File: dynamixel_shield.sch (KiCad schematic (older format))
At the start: 23 parts, among them P1 BARREL_JACK, P2 CONN_01X02, P3 CONN_01X03, P4 CONN_01X03, P5 CONN_01X03, P6 CONN_01X03, P7 CONN_01X03, P8 CONN_01X03, P9 CONN_01X03, Q1 MOSFET_N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

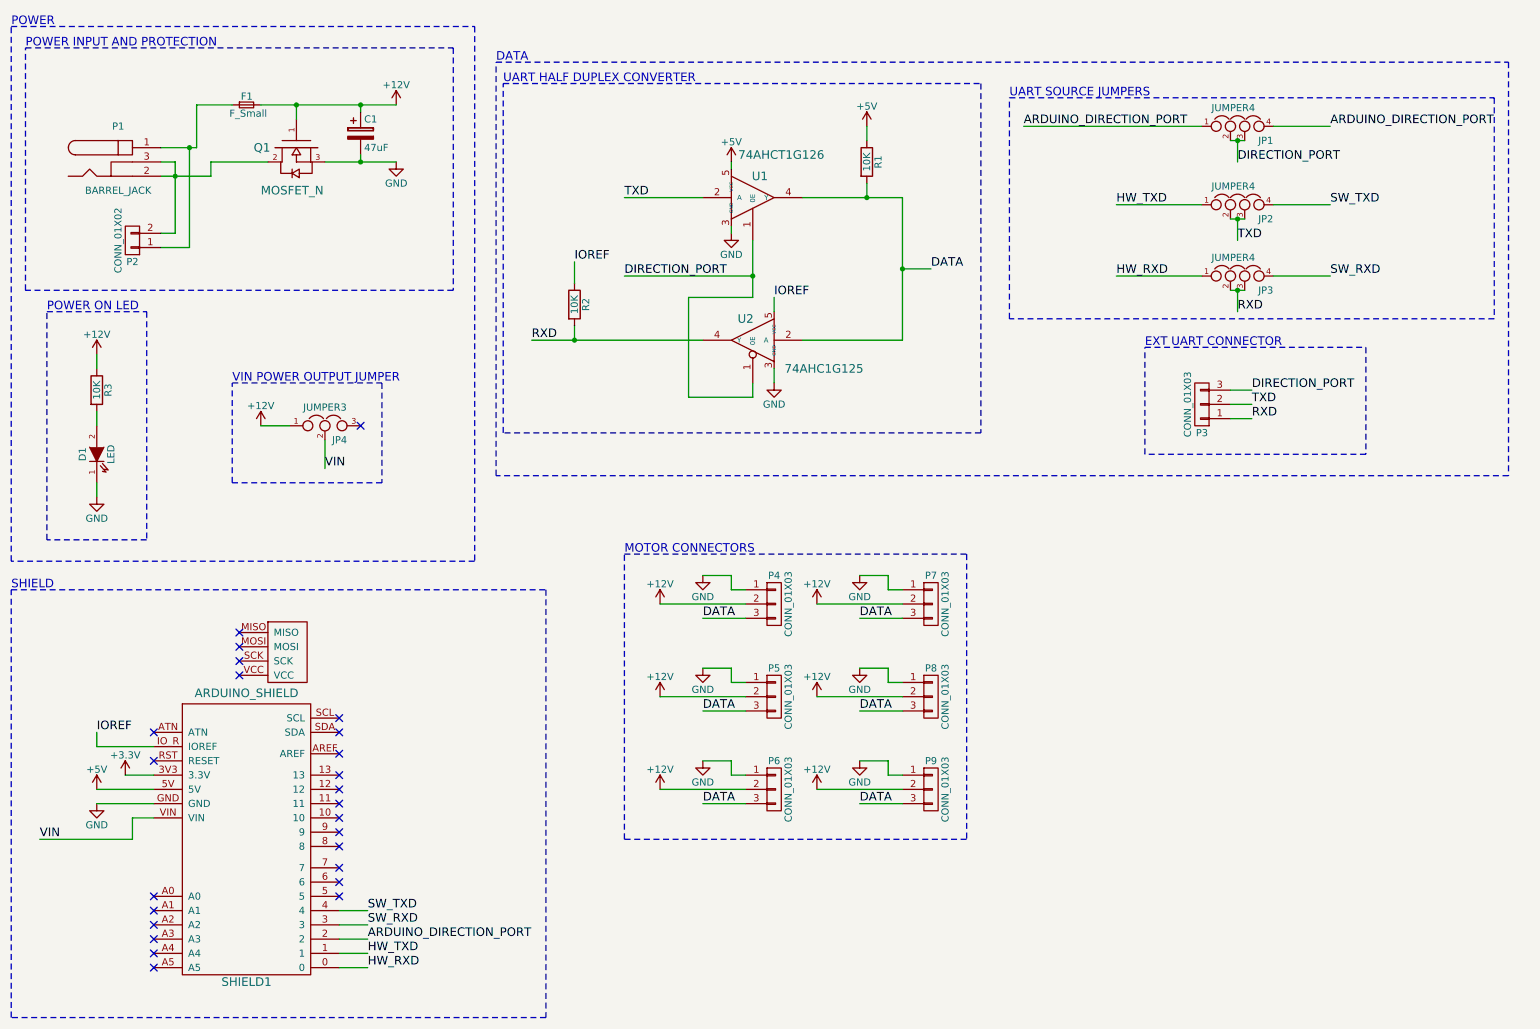
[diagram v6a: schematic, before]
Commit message: add pull up and protection resistor on uart lines
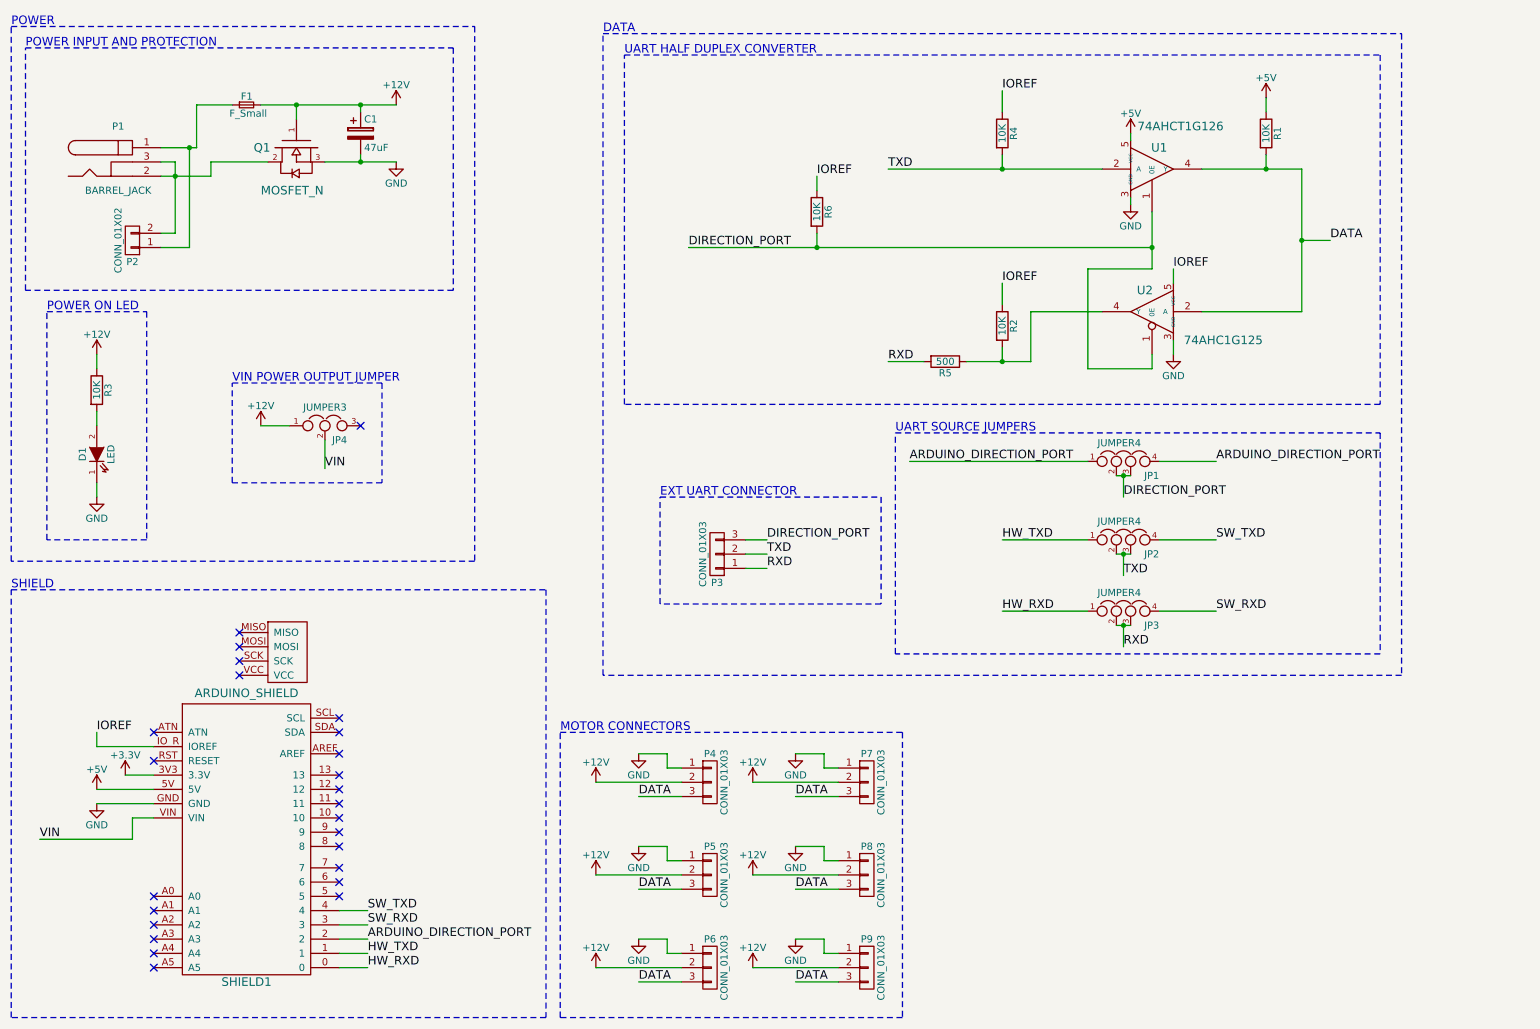
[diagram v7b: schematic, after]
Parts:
- added R4, R6: 10K, Resistors_SMD:R_0603_HandSoldering, symbol R
- added R5: 500, Resistors_SMD:R_0603_HandSoldering, symbol R
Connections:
- net DIRECTION_PORT: now also R6.2
- net IOREF: now also R4.1, R6.1
- net RXD: now also R5.2; no longer R2.2, U2.4 (Y)
- net TXD: now also R4.2
- new net: R2.2, R5.1, U2.4 (Y)
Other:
- moved on the sheet: JP1, JP2, JP3, P3, P4, P5, P6, P7, P8, P9, R1, R2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

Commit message: add optional resistor to set default direction in either rx or tx
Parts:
- added R7: 10K, symbol R
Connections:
- net DIRECTION_PORT: now also R7.1
- net GND: now also R7.2
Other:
- note added: "Note : \nsolder R6 for tx direction by default, \nor R7 for rx direction by default"
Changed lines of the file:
@@
 	6250 1750 6250 1850
 Wire Wire Line
-	6250 2150 6250 2250
+	6250 2150 6250 2400
 Connection ~ 6250 2250
 Wire Notes Line
@@
 Wire Notes Line
 	4750 5250 4750 750
+$Comp
+L R R7
+U 1 1 58023740
+P 6250 2550
+F 0 "R7" V 6330 2550 50  0000 C CNN
+F 1 "10K" V 6250 2550 50  0000 C CNN
+F 2 "" V 6180 2550 50  0000 C CNN
+F 3 "" H 6250 2550 50  0000 C CNN
+	1    6250 2550
+	1    0    0    -1
+$EndComp
+$Comp
+L GND #PWR?
+U 1 1 5802386A
+P 6250 2800
+F 0 "#PWR?" H 6250 2550 50  0001 C CNN
+F 1 "GND" H 6250 2650 50  0000 C CNN
+F 2 "" H 6250 2800 50  0000 C CNN
+F 3 "" H 6250 2800 50  0000 C CNN
+	1    6250 2800
+	1    0    0    -1
+$EndComp
+Wire Wire Line
+	6250 2800 6250 2700
+Text Notes 6450 2150 0    60   ~ 0
+Note : \nsolder R6 for tx direction by default, \nor R7 for rx direction by default
 $EndSCHEMATC
